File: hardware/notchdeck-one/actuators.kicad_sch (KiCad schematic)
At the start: 33 parts, among them J16 SOLENOID 1, J17 SOLENOID 2, J18 ACTIVE BUZZER, J19 EXTERNAL PWM 3V3, Q2 ZXMS6005DGTA, Q3 ZXMS6005DGTA, Q4 ZXMS6005DGTA, Q5 2N7002, U13 TPS259531DSGR

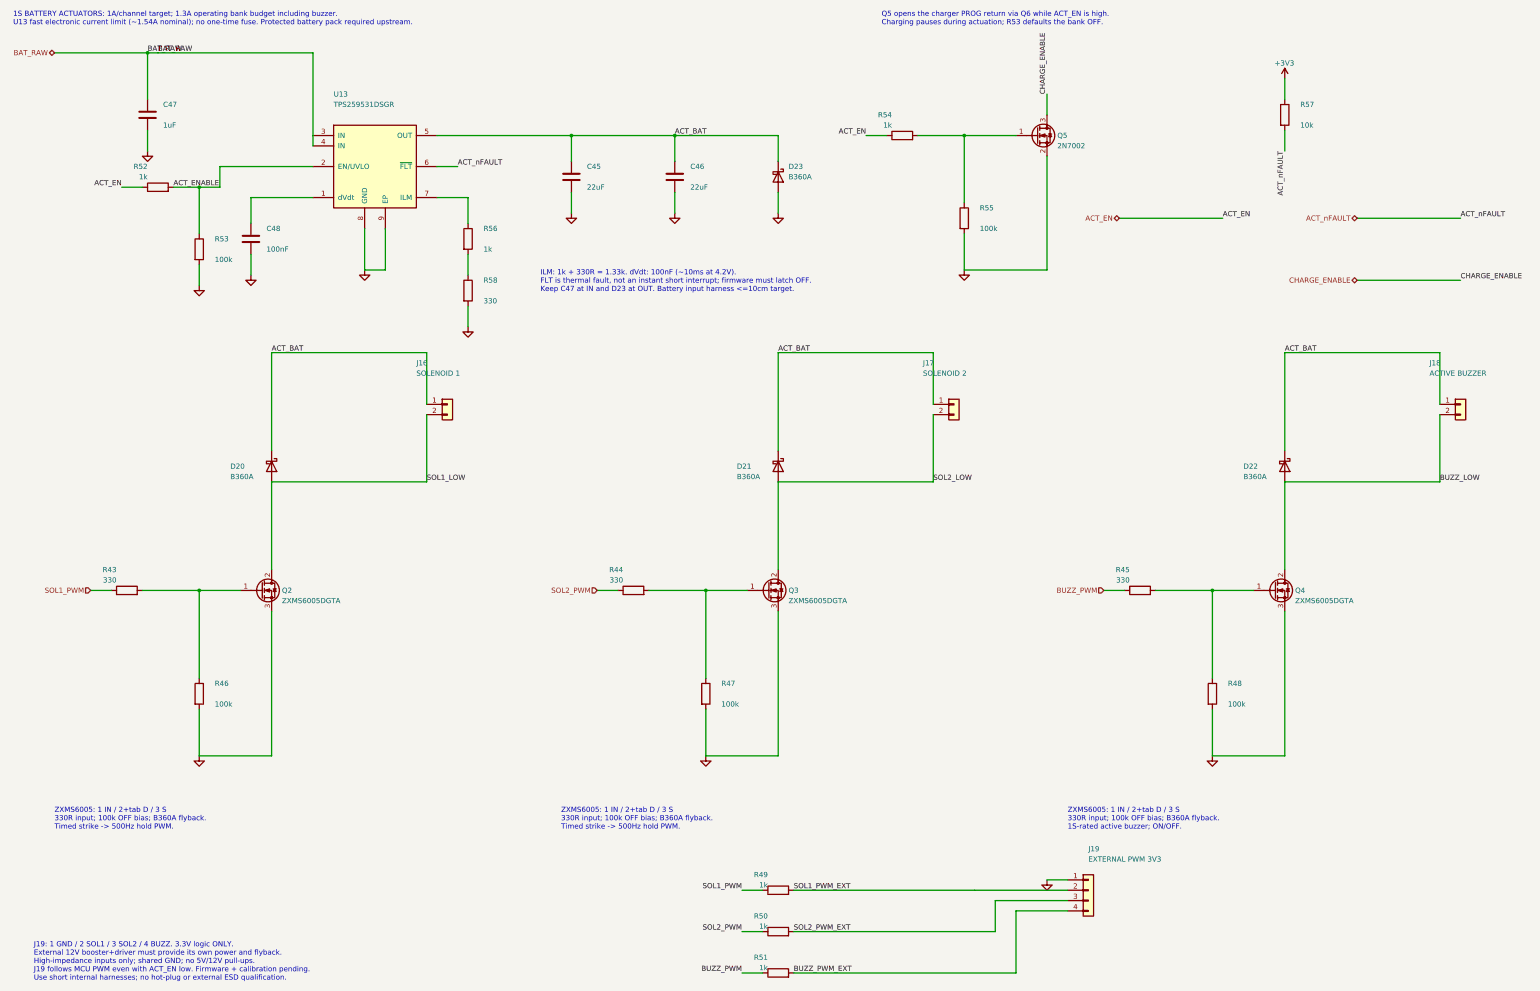
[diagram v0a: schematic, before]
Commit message: Protect full battery input and size dual 2A impulse outputs
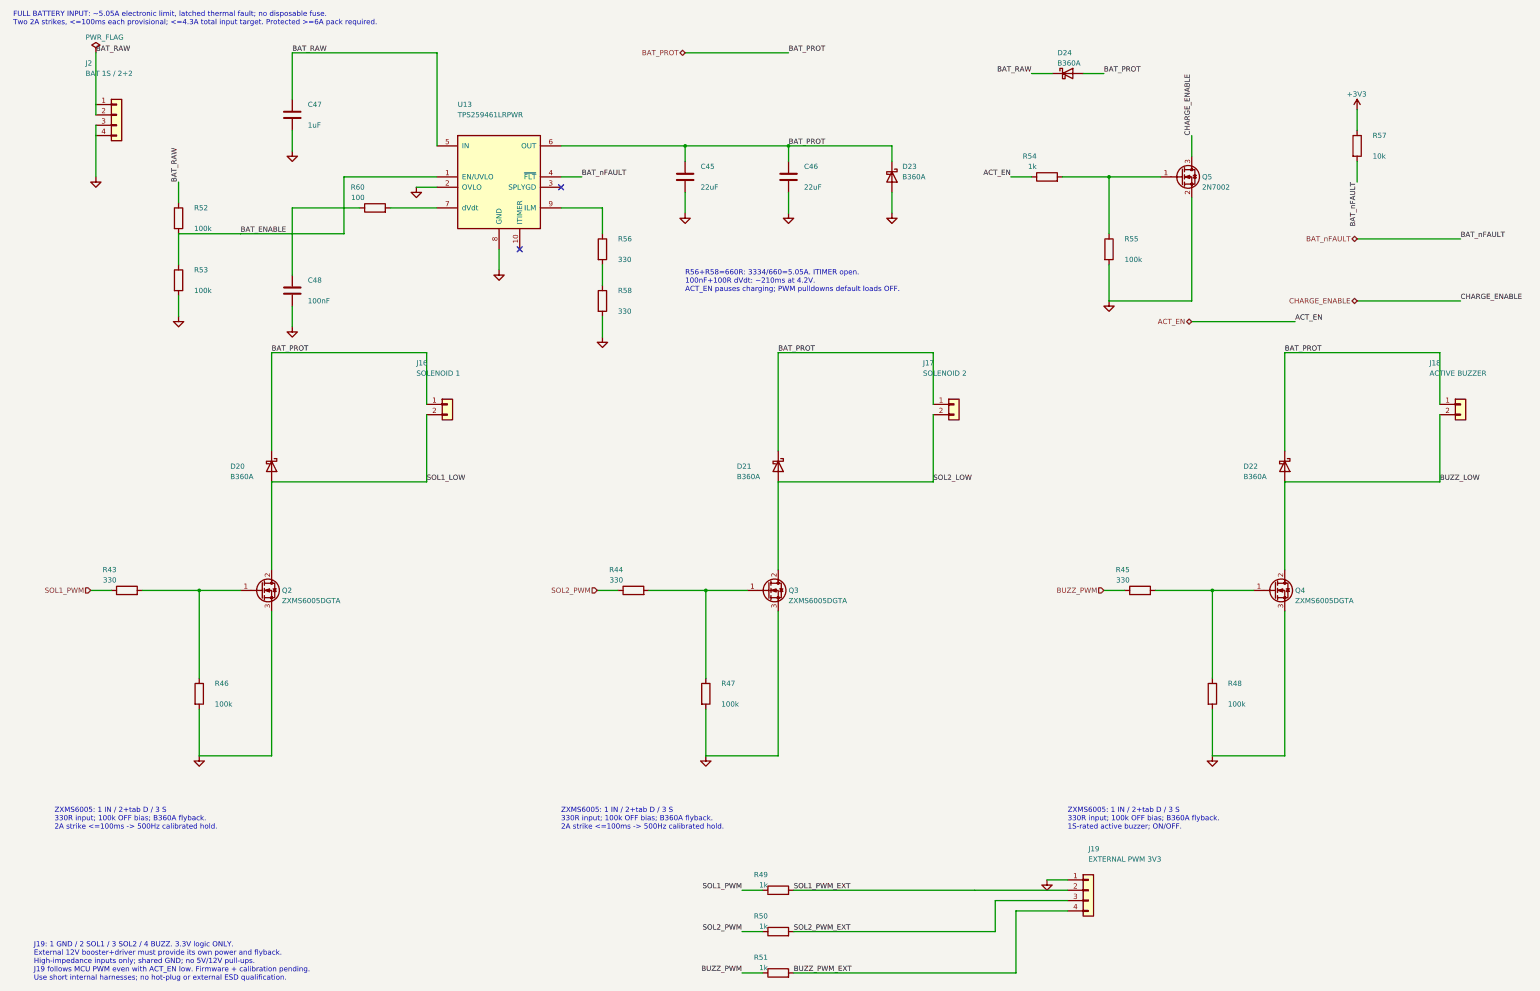
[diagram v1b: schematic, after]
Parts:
- added D24: B360A, Diode_SMD:D_SMA, symbol Device:D_Schottky
- added J2: BAT 1S / 2+2, Connector_Molex:Molex_Micro-Fit_3.0_43045-0400_2x02_P3.00mm_Horizontal, symbol Connector_Generic:Conn_01x04
- added R60: 100, Resistor_SMD:R_0603_1608Metric, symbol Device:R
- D20, D21, D22, D23: BOM Comments 3A/60V Schottky: D20-D22 flyback K=ACT_BAT/A=load negative;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 -> D20-D22 flyback K=BAT_PROT/A=load return; D23 clamp K=BAT_P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
- R52: value 1k -> 100k; BOM Comments -55℃~+155℃ 1kΩ 50V 62.5mW Thick Film Resistor ±1% ±100ppm/℃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 -> -55℃~+155℃ 100kΩ 50V 62.5mW Thick Film Resistor ±1% ±100ppm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; LCSC C11702 -> C25741; MPN 0402WGF1001TCE -> 0402WGF1003TCE
- R56: value 1k -> 330; BOM Comments -55℃~+155℃ 1kΩ 50V 62.5mW Thick Film Resistor ±1% ±100ppm/℃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 -> -55℃~+155℃ 330Ω 50V 62.5mW Thick Film Resistor ±1% ±100ppm/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; LCSC C11702 -> C25104; MPN 0402WGF1001TCE -> 0402WGF3300TCE
- U13: value TPS259531DSGR -> TPS259461LRPWR; footprint Package_DFN_QFN:DFN-8-1EP_2x2mm_P0.5mm_EP0.9x1.6mm -> notchdeck:TI_RPW0010A; symbol notchdeck:TPS259531DSGR -> notchdeck:TPS259461LRPWR; BOM Comments Electronic current limiter, auto-retry; MCU must latch off 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 -> Full battery input electronic limit 5.05A nominal; bidirect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; LCSC C2155674 -> C3662776; MPN TPS259531DSGR -> TPS259461LRPWR; Manufacturer TI -> Texas Instruments
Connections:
- net ACT_EN: no longer R52.1
- net BAT_RAW: now also R52.1, U13.5 (IN), D24.1 (K), J2.1 (Pin_1), J2.2 (Pin_2); no longer U13.3 (IN), U13.4 (IN)
- net GND: now also U13.2 (OVLO), J2.3 (Pin_3), J2.4 (Pin_4); no longer U13.9 (EP)
- net at C48.1: now also R60.1; no longer U13.1 (dVdt)
- net at U13.7 (dVdt): now also R60.2; no longer R56.1
- net ACT_BAT renamed BAT_PROT
- net BAT_PROT: now also U13.6 (OUT), D24.2 (A); no longer U13.5 (OUT)
- net ACT_ENABLE renamed BAT_ENABLE
- net BAT_ENABLE: now also U13.1 (EN/UVLO); no longer U13.2 (EN/UVLO)
- net ACT_nFAULT renamed BAT_nFAULT
- net BAT_nFAULT: now also U13.4 (~{FLT}); no longer U13.6 (~{FLT})
- new net: R56.1, U13.9 (ILM)
- no-connect marks 0 -> 2
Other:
- note added: "FULL BATTERY INPUT: ~5.05A electronic limit, latched thermal fault; no disposable fuse. Two 2A strikes, <=100ms each provisional; <=4.3A total input target. Protected >=6A pack required."
- note added: "R56+R58=660R: 3334/660=5.05A. ITIMER open. 100nF+100R dVdt: ~210ms at 4.2V. ACT_EN pauses charging; PWM pulldowns default loads OFF."
- note added: "ZXMS6005: 1 IN / 2+tab D / 3 S 330R input; 100k OFF bias; B360A flyback. 2A strike <=100ms -> 500Hz calibrated hold."
- note removed: "1S BATTERY ACTUATORS: 1A/channel target; 1.3A operating bank budget including buzzer. U13 fast electronic current limit (~1.54A nominal); no one-time fuse. Protected battery pack required upstream."
- note removed: "ILM: 1k + 330R = 1.33k. dVdt: 100nF (~10ms at 4.2V). FLT is thermal fault, not an instant short interrupt; firmware must latch OFF. Keep C47 at IN and D23 at OUT. Battery input harness <=10cm target."
- note removed: "Q5 opens the charger PROG return via Q6 while ACT_EN is high. Charging pauses during actuation; R53 defaults the bank OFF."
- note removed: "ZXMS6005: 1 IN / 2+tab D / 3 S 330R input; 100k OFF bias; B360A flyback. Timed strike -> 500Hz hold PWM."
- title: NotchDeck One — Solenoids, buzzer and external PWM -> NotchDeck One — Battery protection, solenoids and buzzer
- moved on the sheet: C45, C46, C47, C48, D23, Q5, R52, R53, R54, R55, R56, R57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
